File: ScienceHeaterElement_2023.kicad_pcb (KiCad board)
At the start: 2 copper layers, 5.1 x 119.4 mm, 1 part, among them U1 LMT85DCK

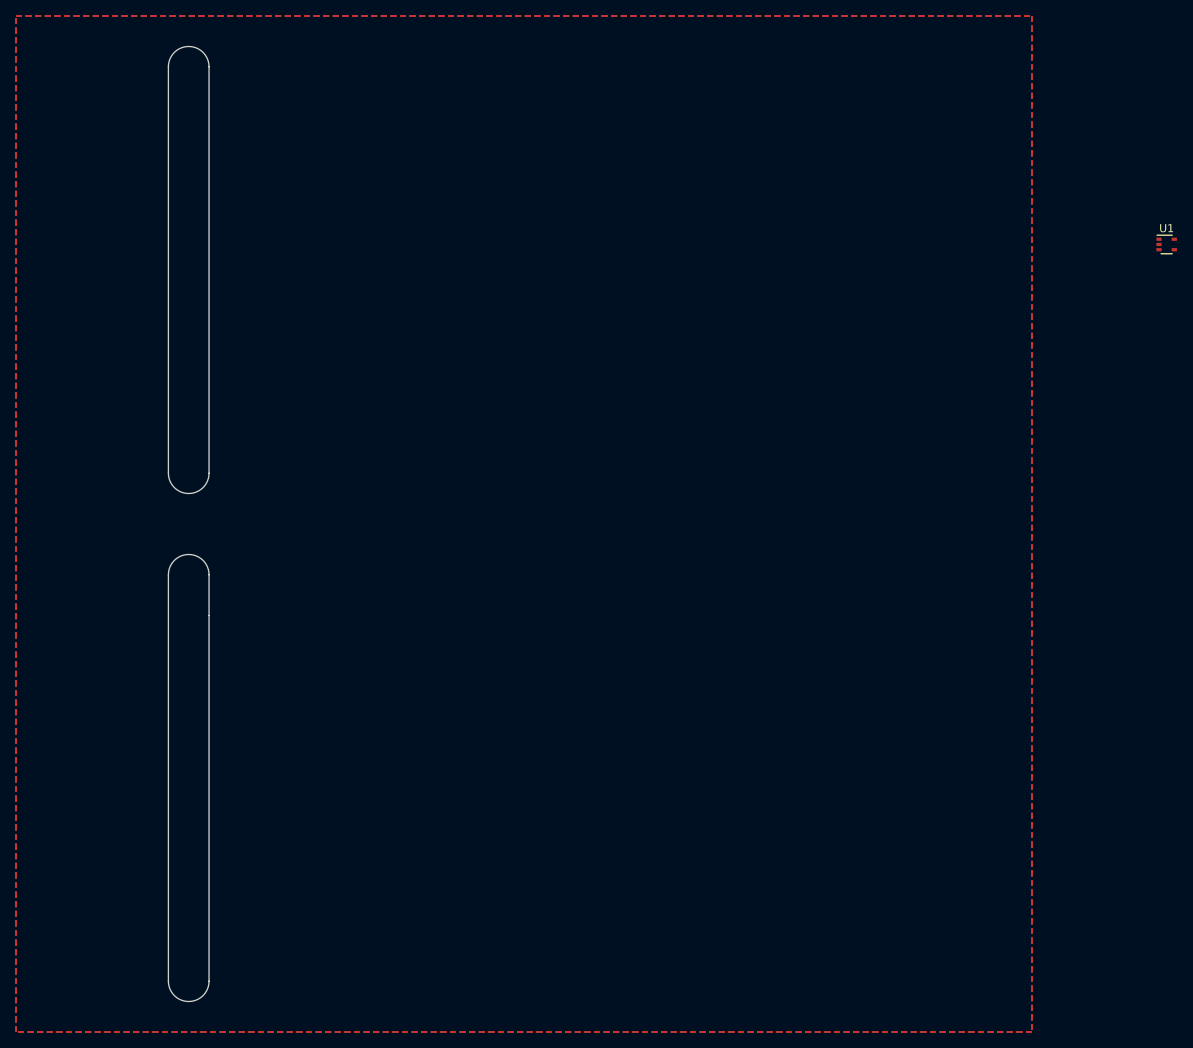
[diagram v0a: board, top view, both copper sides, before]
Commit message: Created PCB traces
Created PCB traces for Science Heater with components placed
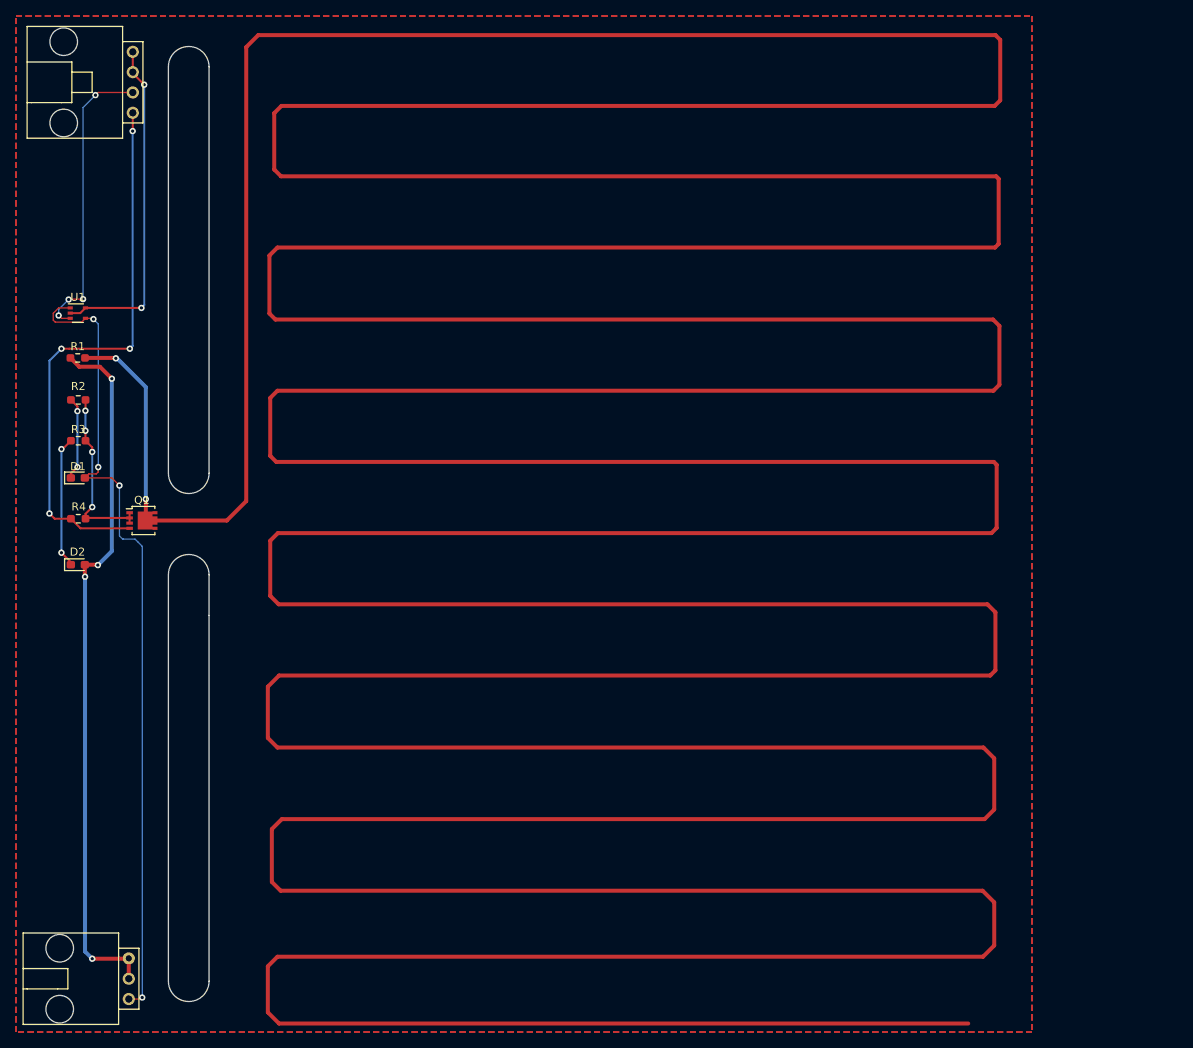
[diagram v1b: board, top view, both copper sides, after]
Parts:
- added Conn1: Molex_SL_03, MRDT_Connectors:MOLEX_SL_03_Horizontal, F.Cu at (85.2, 133.0)
- added Conn2: Molex_SL_04, MRDT_Connectors:MOLEX_SL_04_Horizontal, F.Cu at (85.7, 22.3)
- added D1: Green, LED_SMD:LED_0603_1608Metric_Pad1.05x0.95mm_HandSolder, F.Cu at (78.8, 67.9)
- added D2: Green, LED_SMD:LED_0603_1608Metric_Pad1.05x0.95mm_HandSolder, F.Cu at (78.8, 78.8)
- added Q1: BUK7M6R3-40EX, Package_TO_SOT_SMD:LFPAK33, F.Cu at (86.9, 73.2)
- added R1: 2, Resistor_SMD:R_0603_1608Metric_Pad0.98x0.95mm_HandSolder, F.Cu at (78.8, 52.9)
- added R2: 300, Resistor_SMD:R_0603_1608Metric_Pad0.98x0.95mm_HandSolder, F.Cu at (78.9, 58.1)
- added R3: 1k, Resistor_SMD:R_0603_1608Metric_Pad0.98x0.95mm_HandSolder, F.Cu at (78.9, 63.2)
- added R4: 4.7k, Resistor_SMD:R_0603_1608Metric_Pad0.98x0.95mm_HandSolder, F.Cu at (78.9, 73.0)
- moved U1 136.4 mm to (78.8, 47.3)
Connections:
- net +5V renamed +3.3V
- U1 pad 3: Temp_Sensor -> Temp_Sense
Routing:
- net /Heater_Trace: track 0.00 -> 1567.0 mm, vias 0 -> 2
- net +3.3V: track 0.00 -> 102.5 mm, vias 0 -> 4
- net +12V: track 0.00 -> 88.7 mm, vias 0 -> 4
- net Gate_Driving_Pin: track 0.00 -> 70.2 mm, vias 0 -> 4
- net GND: track 0.00 -> 64.3 mm, vias 0 -> 6
- net Temp_Sense: track 0.00 -> 36.9 mm, vias 0 -> 4
- net Net-(D2-K): track 0.00 -> 16.6 mm, vias 0 -> 2
- net Net-(D1-K): track 0.00 -> 10.4 mm, vias 0 -> 2
